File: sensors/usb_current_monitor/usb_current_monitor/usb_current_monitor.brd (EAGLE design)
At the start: 30.5 x 20.3 mm, 8 parts, among them J1 UJ2-AH-1-SMT-TR, U1 INA169NA/3K

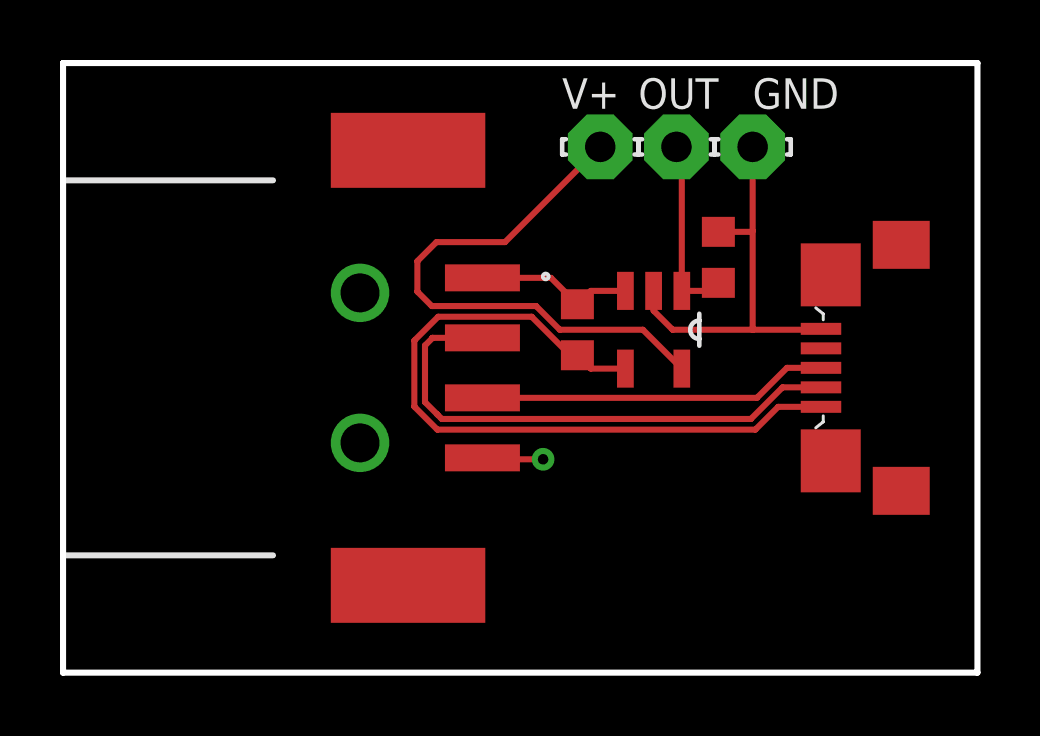
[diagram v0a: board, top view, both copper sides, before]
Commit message: error correction on usb current monitor board
Flipped VIN+ and VIN- on the current sensor to conform with correct direction of current flow
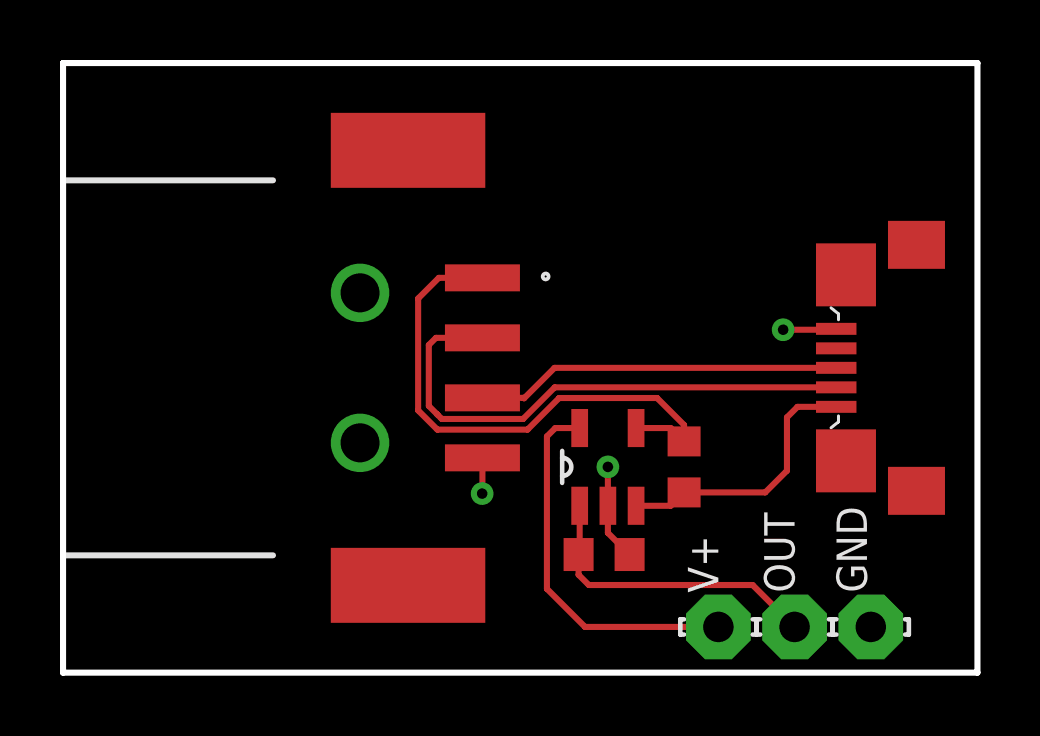
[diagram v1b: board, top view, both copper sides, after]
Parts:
- moved GND 16.5 mm to (26.9, 1.52)
- moved OUT 16.5 mm to (24.4, 1.52)
- moved V+ 16.5 mm to (21.8, 1.52)
- moved RL 10.6 mm to (18.0, 3.94), turned to 180 degrees
- moved RS 5.79 mm to (20.7, 6.86), turned to 270 degrees
- moved U1 4.82 mm to (18.2, 6.86), turned to 90 degrees
- moved U$1 0.51 mm to (28.4, 10.2)
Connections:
- net VCC1: now also U$1.5; no longer J1.1
- net VCC2: now also J1.1; no longer U$1.5
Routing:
- net GND: track 15.8 -> 6.19 mm, vias 1 -> 3
- net VCC2: track 24.5 -> 18.4 mm
- net V+: track 18.6 -> 12.5 mm
- net OUT: track 6.20 -> 10.2 mm
- net VCC1: track 5.31 -> 9.31 mm
- net D+: track 11.7 -> 12.2 mm
